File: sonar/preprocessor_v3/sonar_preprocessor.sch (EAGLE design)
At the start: 29 parts, among them CON4 MOLEX_5566-2, U1 TEENSY_3.1_BASIC, U2 LTC6242, U3 MCP1501, U4 AP7331-20WG-7SOT-5, X1 BN35N61, X2 BN35N61, X3 BN35N61

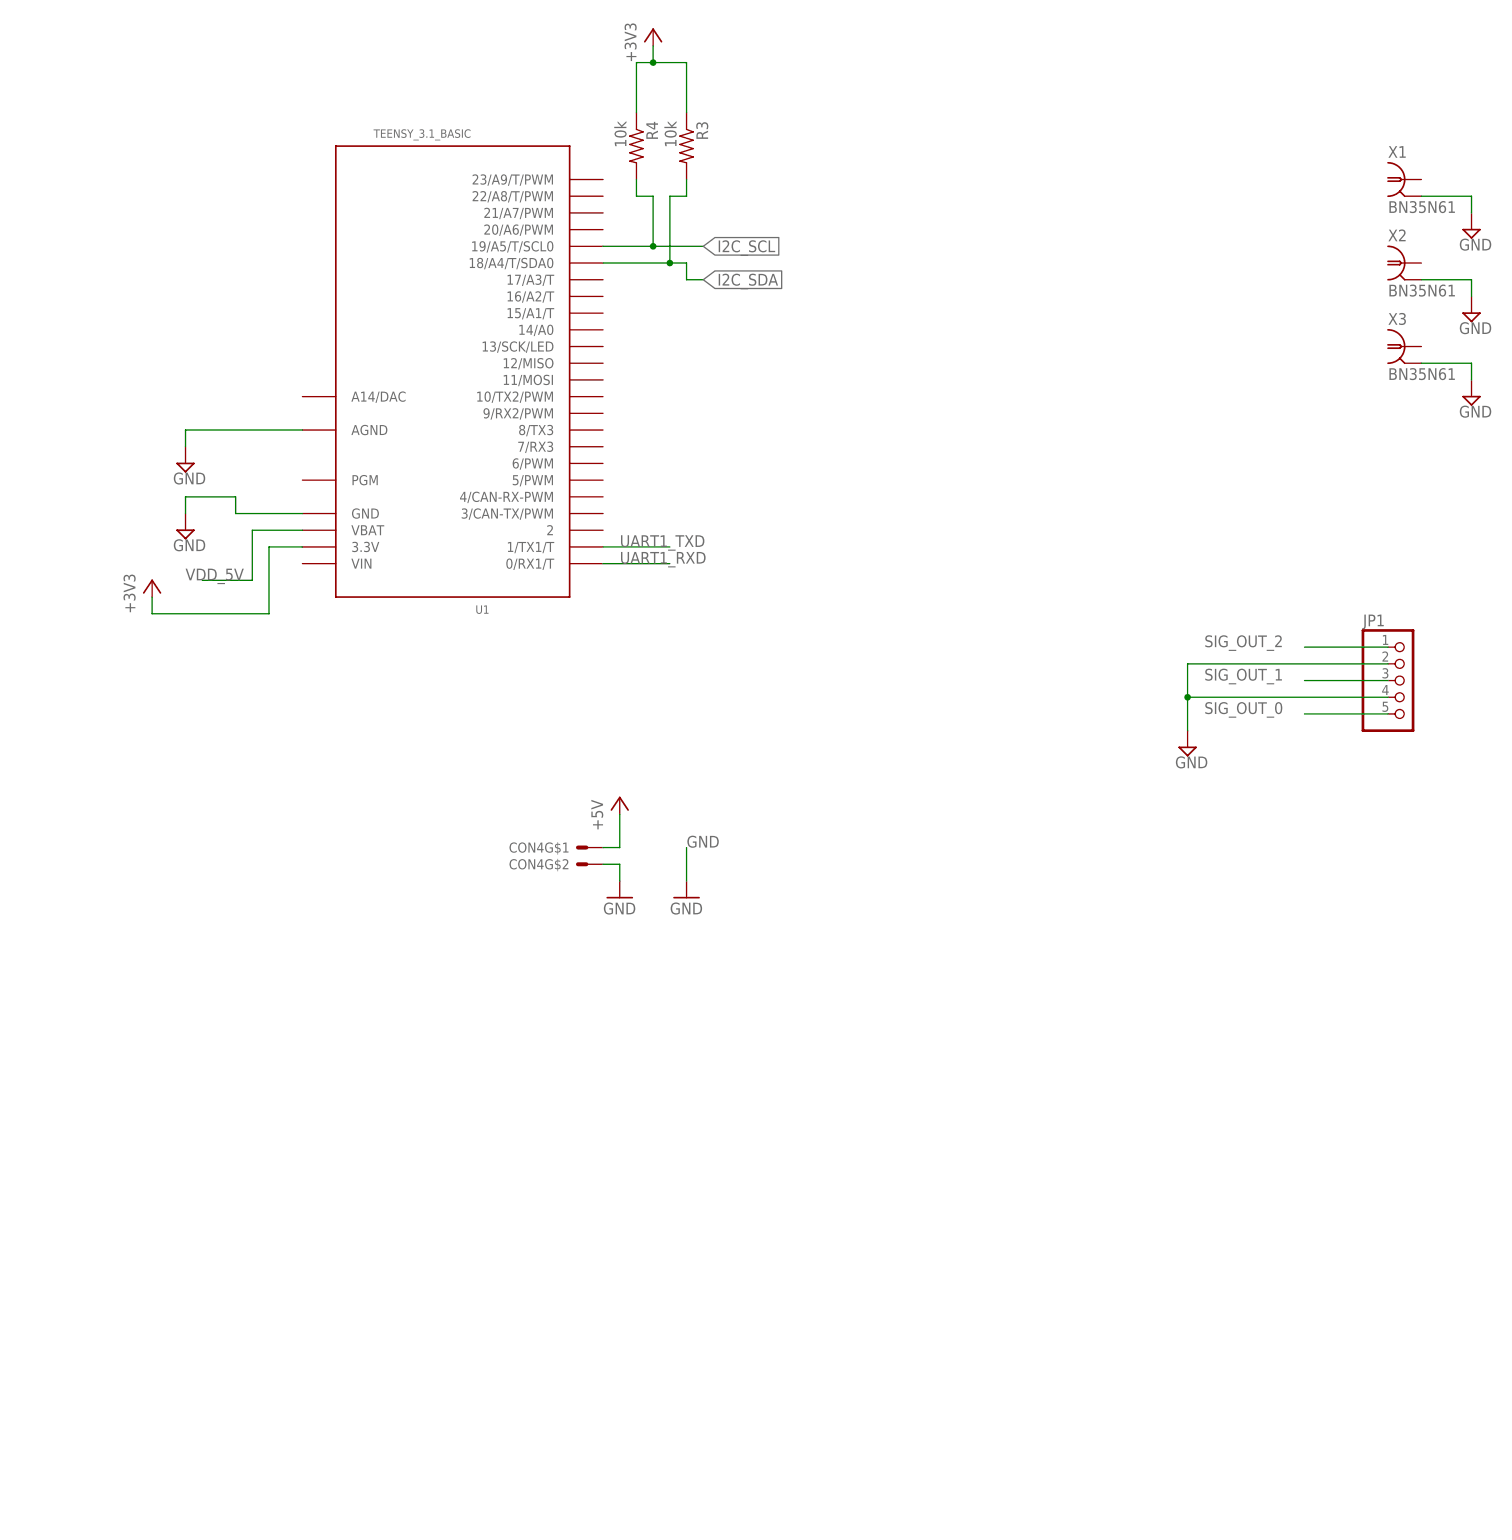
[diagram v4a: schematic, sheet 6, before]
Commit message: Placed power supply, peak detector, filter
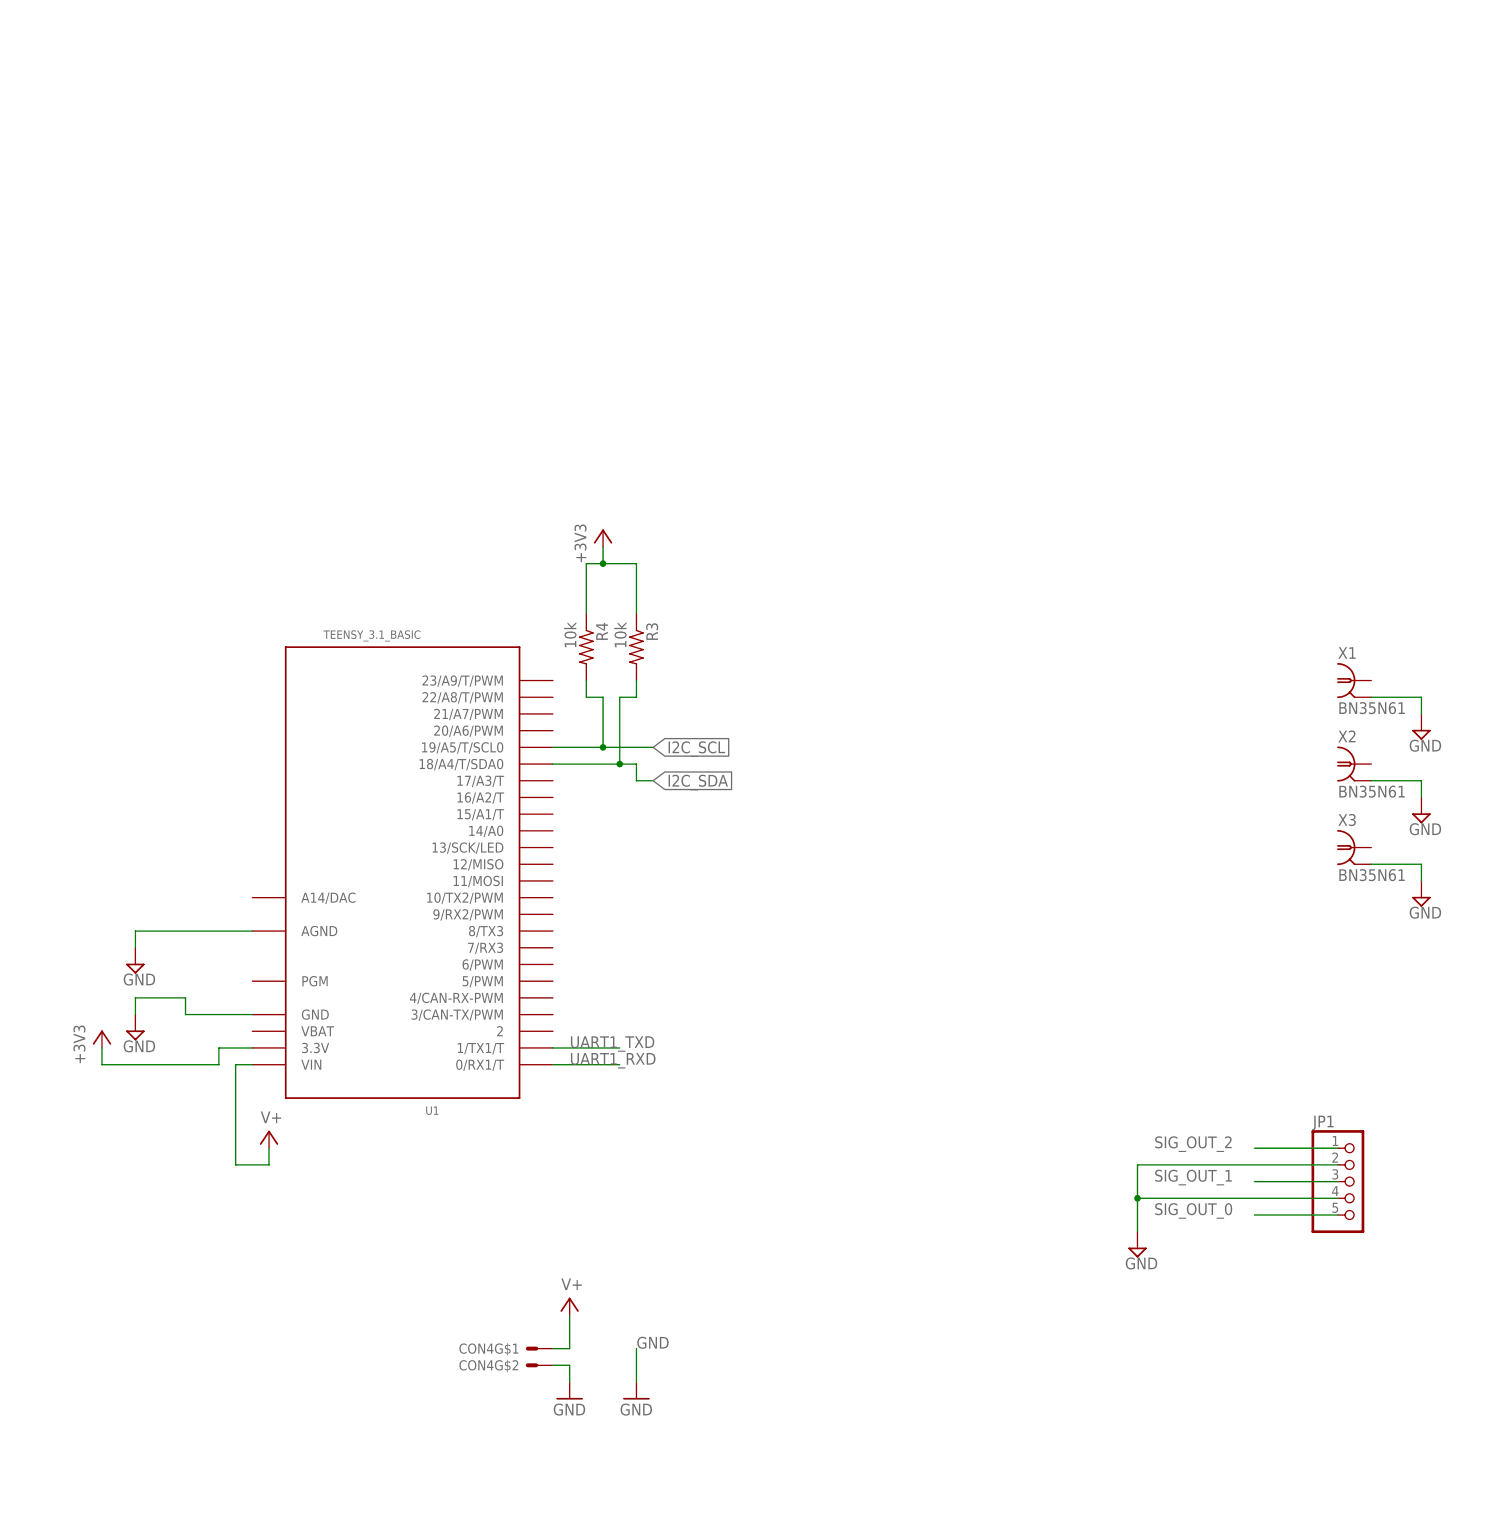
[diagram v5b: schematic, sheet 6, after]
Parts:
- added 25MHZ1: FA-238, ARVP:FA-238
- added C11: 5nF, resistor:C-EUC0805
- added C13, C14, C15, C16: 0.1u, rcl:C-USC0805
- added C17, C18: 0.47u, rcl:C-USC0805
- added C23, C33: 10uF, rcl:C-EUC0805
- added C24, C30: 1uF, rcl:C-EUC1206
- added C25, C34: 10uF, adafruit:C-USC0603
- added C26, C27: 0.33uF, adafruit:C-USC0603
- added C28: 0.33pF, adafruit:C-USC0603
- added C29: 4.7uF, rcl:C-EUC1206
- added C31: 0.1uF, adafruit:C-USC0603
- added C32: 68pF, adafruit:C-USC0603
- added C35: 100uF, rcl:C-EUC1210
- added D1, D2: MBRM120, Moira:MBRM120
- added D4: BAT54S, diode:BAT54S
- added L1: 2.2uH, Moira:LQH5BPN2R2N38L
- added L2: 10uH, Moira:VLS5045EX-100M2
- added L3: 15uH, Moira:VLS5045EX-150M-CA1
- added R16, R19: 10K, resistor:R-EU_R0805
- added R17: 50K, resistor:R-EU_R0805
- added R18: 1K, resistor:R-EU_R0805
- added R1A1, R1A2, R1B1, R1C1, R1D1, R1D2, R3A1, R3A2, R3B1, R3C1, R3D1, R3D2: 350k, rcl:R-US_R0805
- added R20: 150kOhm, adafruit:R-US_R0603
- added R21: 47.5kOhm, adafruit:R-US_R0603
- added R22, R23: 4.7kOhm, adafruit:R-US_R0603
- added R24: 90.9kOhm, adafruit:R-US_R0603
- added R25, R27: 15kOhm, adafruit:R-US_R0603
- added R26: 105kOhm, adafruit:R-US_R0603
- added R2A1, R2A2, R2B1, R2C1, R2D1, R2D2: 10k, rcl:R-US_R0805
- added RCLK1, RCLK2: 200, rcl:R-US_R0805
- added U$6, U$7: LTC1264SMD, ARVP:LTC1264SMD
- added U$8: SI5351A, ARVP:SI5351A
- added U10: LT1117-5, Moira:LT1117-5
- added U11: MMBT3904, MMBT3904:MMBT3904
- added U6: LTC6241, LTC6241:LTC6241
- added U8: LT3471', Moira:LT3471'
- added U9: LT1175, Moira:LT1175
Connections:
- removed net VDD_5V: U1.VBAT
- new net -5V: C13.2, C15.2, C24.1, R21.2, U$6.V-, U$7.V-, U9.OUTPUT
- new net -7.5V: C23.1, C32.2, C33.2, L3.2, R26.1, U9.ILIM2, U9.ILIM4, U9.VIN, U9.VIN2
- new net 7.5V: C28.1, C29.1, C34.1, D2.C, R24.2, U10.IN
- new net CLEAR: R19.1
- new net CLK0: U$8.CLK0
- new net CLK1: RCLK1.2, U$8.CLK1
- new net CLK2: RCLK2.2, U$8.CLK2
- new net IN: U6G1.+IN
- new net IN_1: R1A1.1
- new net IN_2: R1B1.1
- new net IN_3: R1A2.1
- new net N$1: R20.2, R21.1, U9.SENSE
- new net N$10: 25MHZ1.XB, U$8.XB
- new net N$12: C11.1, D4.C2, R17.2, R18.2, U6G2.+IN
- new net N$13: D4.A1, R16.1, U6G1.-IN
- new net N$14: D4.C1A2, U6G1.OUT
- new net N$15: R19.2, U11.B
- new net N$16: R18.1, U11.C
- new net N$2: D2.A, L1.2, U8.SW1
- new net N$24: R2A1.2, U$6.HPA/NA
- new net N$25: U$6.LPA, U$6.SA
- new net N$26: R1A1.2, R2A1.1, R3A1.1, U$6.INVA
- new net N$27: R2D1.2, U$6.HPD/ND
- new net N$28: R1D1.2, R2D1.1, R3D1.1, U$6.INVD
- new net N$29: U$6.LPD, U$6.SD
- new net N$3: C28.2, R24.1, R25.2, U8.FB1N
- new net N$30: R2C1.1, U$6.HPC/NC
- new net N$31: R1C1.1, R2C1.2, R3C1.2, U$6.INVC
- new net N$33: R2B1.2, U$6.HPB/NB
- new net N$34: R1B1.2, R2B1.1, R3B1.1, U$6.INVB
- new net N$35: U$6.LPB, U$6.SB
- new net N$36: U$6.LPC, U$6.SC
- new net N$37: RCLK1.1, U$6.CLK
- new net N$38: R2A2.2, U$7.HPA/NA
- new net N$39: U$7.LPA, U$7.SA
- new net N$4: C30.1, L2.2, U8.SW2
- new net N$40: R1A2.2, R2A2.1, R3A2.1, U$7.INVA
- new net N$41: R2D2.2, U$7.HPD/ND
- new net N$42: R1D2.2, R2D2.1, R3D2.1, U$7.INVD
- new net N$43: U$7.LPD, U$7.SD
- new net N$48: U$7.LPB, U$7.SB
- new net N$49: U$7.LPC, U$7.SC
- new net N$5: C30.2, D1.A, L3.1
- new net N$50: RCLK2.1, U$7.CLK
- new net N$6: C32.1, R26.2, R27.1, U8.FB2P
- new net N$9: 25MHZ1.XA, U$8.XA
- new net OUT: R16.2, R17.1, U6G2.-IN, U6G2.OUT
- new net OUT_1: R3D1.2, U$6.BPD
- new net OUT_2: R3C1.1, U$6.BPC
- new net OUT_2ND_A1: R1D1.1, R3A1.2, U$6.BPA
- new net OUT_2ND_A2: R1D2.1, R3A2.2, U$7.BPA
- new net OUT_2ND_ORDER_B1: R1C1.2, R3B1.2, U$6.BPB
- new net OUT_3: R3D2.2, U$7.BPD
- new net SCL: U$8.SCL
- new net SDA: U$8.SDA
- new net SS3: C26.1, R22.1, U8.SHDN/SS2
- new net SS4: C27.1, R23.1, U8.SHDN/SS1
- new net V+: C25.1, CON4G$1.S, L1.1, L2.1, R22.2, R23.2, U1.VIN, U8.VIN
- new net VDD: C17.1, C18.1, U$8.VDD, U$8.VDDO
- new net VREF: C31.1, R27.2, U8.FB1P, U8.VREF
- net +5V: now also C14.1, C16.1, C35.1, U$6.V+, U$7.V+, U10.OUT, U10.VOUT, U6G3.V+; no longer CON4G$1.S
- net GND: now also C11.2, C13.1, C14.2, C15.1, C16.2, C17.2, C18.2, C23.2, C24.2, C25.2, C26.2, C27.2, C29.2, C31.2, C33.1, C34.2, C35.2, D1.C, R20.1, R25.1, U$6.AGND, U$7.AGND, U$8.GND, U10.GND/ADJ, U11.E, U6G3.V-, U8.FB2N, U8.GND, U9.GND
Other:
- note added: "1) Do not use Vias to connect the supply cap to VDD/VDDO 2) Leave a ground plane direrectly under the crystal 3)Attach driver clock directly to filter, attach a 2nd clock to an external test pin"
- moved on the sheet: CON4G$1, CON4G$2, JP1, R3, R4, U1, X1, X2, X3

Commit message: Routing and layout work
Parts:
- added C12: 100n, rcl:C-EUC0805
- added C19, C20: 1u, rcl:C-EUC0805
- added C2: 100n, resistor:C-EUC0805
- added C50, C52, C54, C56, C58, C60, C62, C64, C66, C68, C69: 0.1uF, rcl:C-EUC0603
- added C51, C53, C57, C59, C63, C65: 10uF, resistor:C-EUC1206
- added C55, C61, C67: 1nF, rcl:C-EUC0603
- added JP2, JP3: (no value), pinhead-2:PINHD-1X03_2.54-SMD-90°
- added JP4: (no value), pinhead:PINHD-1X2
- added L10, L13, L14, L15, L6, L9: 120nH, resistor:L-USL3225P
- added R30, R32, R34: 1.9k, rcl:R-US_R0603
- added R31, R33, R35: 100, rcl:R-US_R0603
- added TP1, TP2, TP3, TP4, TP5, TP6, TP7, TP8, TP9: TPB2,54, testpad:TPB2,54
- added U14, U15, U16: AD8336ACPZ-R7, Amplifier-Sonar-LBR:AD8336ACPZ-R7
- added U17: ISL21080DIH309Z-TK, Amplifier-Sonar-Prototype-LBR:ISL21080DIH309Z-TK
- added U5: MCP1501, ARVP:MCP1501
- C11: value 5nF -> 5n
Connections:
- net CLEAR renamed PEAK_CLEAR
- net IN renamed PEAK_IN
- removed net FILTER_OUT_0: C8.2
- removed net IN_1: R1A1.1
- removed net IN_2: R1B1.1
- removed net IN_3: R1A2.1
- removed net OUT: R16.2, R17.1, U6G2.-IN, U6G2.OUT
- removed net OUT_1: R3D1.2, U$6.BPD
- removed net OUT_2: R3C1.1, U$6.BPC
- removed net OUT_3: R3D2.2, U$7.BPD
- removed net SCL: U$8.SCL
- removed net SDA: U$8.SDA
- removed net VDD: C17.1, C18.1, U$8.VDD, U$8.VDDO
- new net 2V5_REF: C12.1, C19.1, U1.AREF, U5.OUT
- new net AMP_1: R1A1.1, TP4.TP, U14.VOUT
- new net AMP_2: R1B1.1, TP5.TP, U15.VOUT
- new net AMP_3: R1A2.1, TP6.TP, U16.VOUT
- new net FILTER_OUT_3: C10.2, R3D2.2, TP9.TP, U$7.BPD
- new net GAIN_NEG: C54.1, C60.1, C66.1, C69.1, U14.GNEG, U15.GNEG, U16.GNEG, U17.VOUT
- new net GAIN_POS: C55.1, C61.1, C67.1, U1.A14/DAC, U14.GPOS, U15.GPOS, U16.GPOS
- new net GPIO_0: JP3.1, U1.12/MISO
- new net INPN1: R30.2, R31.1, U14.INPN
- new net INPN2: R32.2, R33.1, U15.INPN
- new net INPN3: R34.2, R35.1, U16.INPN
- new net INPUT1: TP1.TP, U14.INPP, X1.1
- new net INPUT2: TP2.TP, U15.INPP, X2.1
- new net INPUT3: TP3.TP, U16.INPP, X3.1
- new net N$7: U$7.SC
- new net N$8: U$7.SB
- new net PEAK_OUT: R16.2, R17.1, U1.23/A9/T/PWM, U6G2.-IN, U6G2.OUT
- new net VGA_INPUT1: R30.1, U14.PRAO, U14.VGAI
- new net VGA_INPUT2: R32.1, U15.PRAO, U15.VGAI
- new net VGA_INPUT3: R34.1, U16.PRAO, U16.VGAI
- new net VNEG1: C50.1, L6.1, U14.VNEG
- new net VNEG2: C56.1, L10.1, U15.VNEG
- new net VNEG3: C62.1, L14.1, U16.VNEG
- new net VPOS1: C52.1, L9.1, U14.VPOS
- new net VPOS2: C58.1, L13.1, U15.VPOS
- new net VPOS3: C64.1, L15.1, U16.VPOS
- net +3V3: now also C17.1, C18.1, U$8.VDD, U$8.VDDO
- net +5V: now also C2.1, C53.1, C59.1, C65.1, C68.1, L13.2, L15.2, L9.2, U17.VIN
- net -5V: now also C51.1, C57.1, C63.1, L10.2, L14.2, L6.2
- net CLK0: now also RCLK1.2
- net CLK1: now also RCLK2.2; no longer RCLK1.2
- net CLK2: no longer RCLK2.2
- net FILTER_OUT_1: now also C8.2, R3D1.2, TP7.TP, U$6.BPD; no longer C9.2
- net FILTER_OUT_2: now also C9.2, R3C1.1, TP8.TP, U$6.BPC; no longer C10.2
- net GND: now also C12.2, C19.2, C2.2, C20.2, C50.2, C51.2, C52.2, C53.2, C54.2, C55.2, C56.2, C57.2, C58.2, C59.2, C60.2, C61.2, C62.2, C63.2, C64.2, C65.2, C66.2, C67.2, C68.2, C69.2, JP2.3, JP4.1, JP4.2, R31.2, R33.2, R35.2, U14.EP, U14.NC, U14.NC_2, U14.NC_3, U14.NC_4, U14.NC_5, U14.PWRA, U14.VCOM, U15.EP, U15.NC, U15.NC_2, U15.NC_3, U15.NC_4, U15.NC_5, U15.PWRA, U15.VCOM, U16.EP, U16.NC, U16.NC_2, U16.NC_3, U16.NC_4, U16.NC_5, U16.PWRA, U16.VCOM, U17.GND, U5.GND
- net I2C_SCL: now also JP3.2, U$8.SCL
- net I2C_SDA: now also JP3.3, U$8.SDA
- net N$48: no longer U$7.SB
- net N$49: no longer U$7.SC
- net UART1_RXD: now also JP2.2
- net UART1_TXD: now also JP2.1
- net V+: now also C20.1, U5./SHDN, U5.VDD
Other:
- note added: "Keep close to IC"
- note added: "Noise Filter for Gain Control"
- note added: "Noise Filter for Gain Control Close to IC"
- note added: "Power Filters"
- note added: "Pre-Amp Gain 20x(+26dB)"
- note added: "Pre-Amp Gain: R1/R2 + 1"
- note added: "VGA Gain(dB) = (Vgain * 50dB)+4.4dB Vgain = GAIN_POS - GAIN_NEG Pre-Amplifier Gain = +26dB Total Gain: ( (GAIN_POS - GAIN_NEG) * 50dB) + 30.4dB"
- note added: "VGAIN = GAIN_POS - GAIN_NEG -0.6V < VGAIN < 0.6V Total Gain = VGAIN + Pre-Amp Gain 0.4dB < Total Gain < 60.4dB"
- note added: "Voltage Bias for VNEG 0.9V"
- moved on the sheet: 25MHZ1, C13, C14, C15, C16, C17, C18, CON4G$1, CON4G$2, R1A1, R1A2, R1B1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
